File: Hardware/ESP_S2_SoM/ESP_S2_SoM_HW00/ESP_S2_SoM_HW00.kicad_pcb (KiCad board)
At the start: 2 copper layers, 21 x 26 mm, 53 parts, among them J101 USB4510-03-1-A, J102 54722-0604, SW401 SW_Push, SW402 SW_Push, U201 BQ24075RGTR, U301 MIC5528-3.3YMT-T5, U401 ESP32-S2FH4, Y601 Crystal_GND24_Small

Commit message: working on schematic
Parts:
- moved TP201 39.0 mm to (178.0, 49.0)
- moved SW401 16.3 mm to (176.7, 31.5)
- moved SW402 16.3 mm to (176.7, 35.2)
- moved Y601 16.3 mm to (177.7, 38.2)
- moved ANT401 16.3 mm to (171.0, 35.0)
- moved C409 16.3 mm to (174.6, 38.1)
- moved J101 11.2 mm to (158.6, 37.0)
- moved U401 1.41 mm to (161.1, 47.3), turned to -90 degrees
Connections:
- J102 pad 17: unconnected-(J102-Pad17) -> GND
- J102 pad 19: unconnected-(J102-Pad19) -> /100_Connectors/SPID
- J102 pad 21: unconnected-(J102-Pad21) -> /100_Connectors/SPIQ
- J102 pad 23: unconnected-(J102-Pad23) -> /100_Connectors/SPICLK
- J102 pad 25: unconnected-(J102-Pad25) -> /100_Connectors/SPICS0
- J102 pad 27: unconnected-(J102-Pad27) -> /100_Connectors/SPIWP
- J102 pad 29: unconnected-(J102-Pad29) -> /100_Connectors/SPIHD
- J102 pad 31: unconnected-(J102-Pad31) -> /100_Connectors/VDD_SPI
- J102 pad 33: unconnected-(J102-Pad33) -> /100_Connectors/SPICS1
- J102 pad 35: unconnected-(J102-Pad35) -> GND
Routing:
- net /400_ESP32/SPIHD: track 0.00 -> 2.73 mm, vias 0 -> 1
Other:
- copper layers 2 -> 4

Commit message: lots of work on routing
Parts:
- removed TP201: TestPoint, TestPoint:TestPoint_Pad_D1.0mm
- added R1: R, Resistor_SMD:R_0402_1005Metric, F.Cu at (156.2, 52.4)
- added REF**: usb-c-pcb, Component_lib:usb-c-pcb, B.Cu at (166.1, 32.1)
- C403, C404, C405, C408, C411, C412, C414, C415, C416: footprint Capacitor_SMD:C_0402_1005Metric -> Capacitor_SMD:C_0201_0603Metric
- R101, R102: moved to B.Cu
- moved U301 19.9 mm to (155.7, 55.6), turned to 180 degrees
- moved C413 19.7 mm to (173.6, 53.5), turned to -90 degrees
- moved C412 18.9 mm to (172.7, 53.3), turned to -90 degrees
- moved C301 18.8 mm to (153.7, 55.7), turned to 90 degrees
- moved R201 18.7 mm to (155.8, 44.3)
- moved R202 18.6 mm to (155.8, 43.4)
- moved C409 18.5 mm to (161.7, 51.4), turned to -90 degrees
- moved R203 18.5 mm to (154.4, 45.9)
- moved R301 17.9 mm to (155.3, 54.3), turned to 180 degrees
- moved R101 17.5 mm to (156.7, 42.4), turned to 180 degrees
- moved C201 17.1 mm to (154.2, 48.3), turned to 90 degrees
- moved C403 16.9 mm to (170.8, 45.6), turned to 90 degrees
- moved C416 16.8 mm to (170.7, 55.3)
- moved C402 16.4 mm to (169.0, 43.3), turned to -90 degrees
- moved C202 15.4 mm to (157.0, 45.6), turned to 180 degrees
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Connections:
- C412 pad 1: /400_ESP32/VDD_SPI -> SPI6
- C413 pad 1: /400_ESP32/VDD_SPI -> SPI6
- J102 pad 11: GND -> /100_Connectors/BATTERY_TEMP
- J102 pad 13: /100_Connectors/RX0 -> GND
- J102 pad 15: /100_Connectors/TX0 -> /100_Connectors/RX0
- J102 pad 17: GND -> /100_Connectors/TX0
- J102 pad 19: /100_Connectors/SPID -> GND
- J102 pad 21: /100_Connectors/SPIQ -> SPI0
- J102 pad 23: /100_Connectors/SPICLK -> SPI1
- J102 pad 25: /100_Connectors/SPICS0 -> SPI2
- J102 pad 27: /100_Connectors/SPIWP -> SPI3
- J102 pad 29: /100_Connectors/SPIHD -> SPI4
- J102 pad 31: /100_Connectors/VDD_SPI -> SPI5
- J102 pad 33: /100_Connectors/SPICS1 -> SPI6
- J102 pad 35: GND -> SPI7
- J102 pad 37: IO34 -> GND
- J102 pad 39: IO35 -> IO34
- J102 pad 41: IO36 -> IO35
- J102 pad 43: IO37 -> IO36
- J102 pad 45: IO38 -> IO37
- J102 pad 47: IO39 -> IO38
- J102 pad 49: IO40 -> IO39
- J102 pad 51: IO41 -> IO40
- J102 pad 53: IO42 -> IO41
- J102 pad 54: IO33 -> GND
- J102 pad 55: GND -> IO42
- J102 pad 56: GND -> /100_Connectors/D-
- J102 pad 57: /100_Connectors/D- -> IO33
- U201 pad 1: /200_1S_Charger/BATTERY_TEMP -> /100_Connectors/BATTERY_TEMP
- U401 pad 29: /400_ESP32/SPICS1 -> SPI7
- U401 pad 30: /400_ESP32/VDD_SPI -> SPI6
- U401 pad 31: /400_ESP32/SPIHD -> SPI5
- U401 pad 32: /400_ESP32/SPIWP -> SPI4
- U401 pad 33: /400_ESP32/SPICS0 -> SPI3
- U401 pad 34: /400_ESP32/SPICLK -> SPI2
- U401 pad 35: /400_ESP32/SPIQ -> SPI1
- U401 pad 36: /400_ESP32/SPID -> SPI0
- Y601 pad 1: Net-(C401-Pad1) -> Net-(U401-XTAL_N)
- Y601 pad 3: Net-(U401-XTAL_N) -> Net-(C401-Pad1)
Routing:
- net IO0: track 0.00 -> 9.94 mm
- net IO1: track 0.00 -> 9.30 mm
- net IO2: track 0.00 -> 8.79 mm
- net IO3: track 0.00 -> 8.29 mm
- net IO4: track 0.00 -> 7.79 mm
- net +3V3: track 0.00 -> 7.35 mm, vias 0 -> 1
- net IO5: track 0.00 -> 7.29 mm
- net IO6: track 0.00 -> 6.78 mm
- net IO7: track 0.00 -> 6.28 mm
- net IO8: track 0.00 -> 5.77 mm
- net GND: track 0.00 -> 5.26 mm
- net IO9: track 0.00 -> 5.23 mm
- net Net-(U401-XTAL_N): track 0.00 -> 4.75 mm
- net /200_1S_Charger/TMR: track 0.00 -> 4.38 mm
- net /200_1S_Charger/VSYS: track 0.00 -> 3.41 mm
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- added copper zone on In1.Cu, net GND
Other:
- board size 21 x 26 mm -> 22 x 25.6 mm

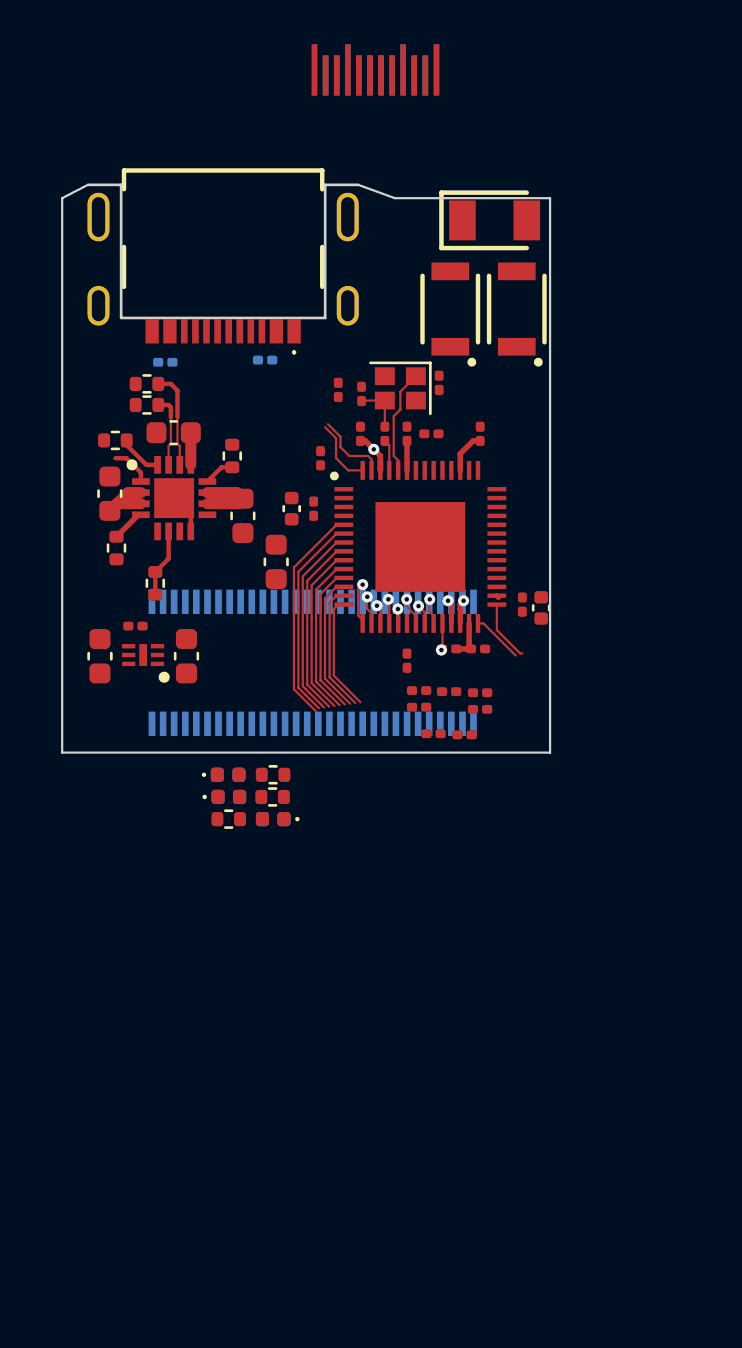
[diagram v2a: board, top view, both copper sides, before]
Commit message: led footprint update
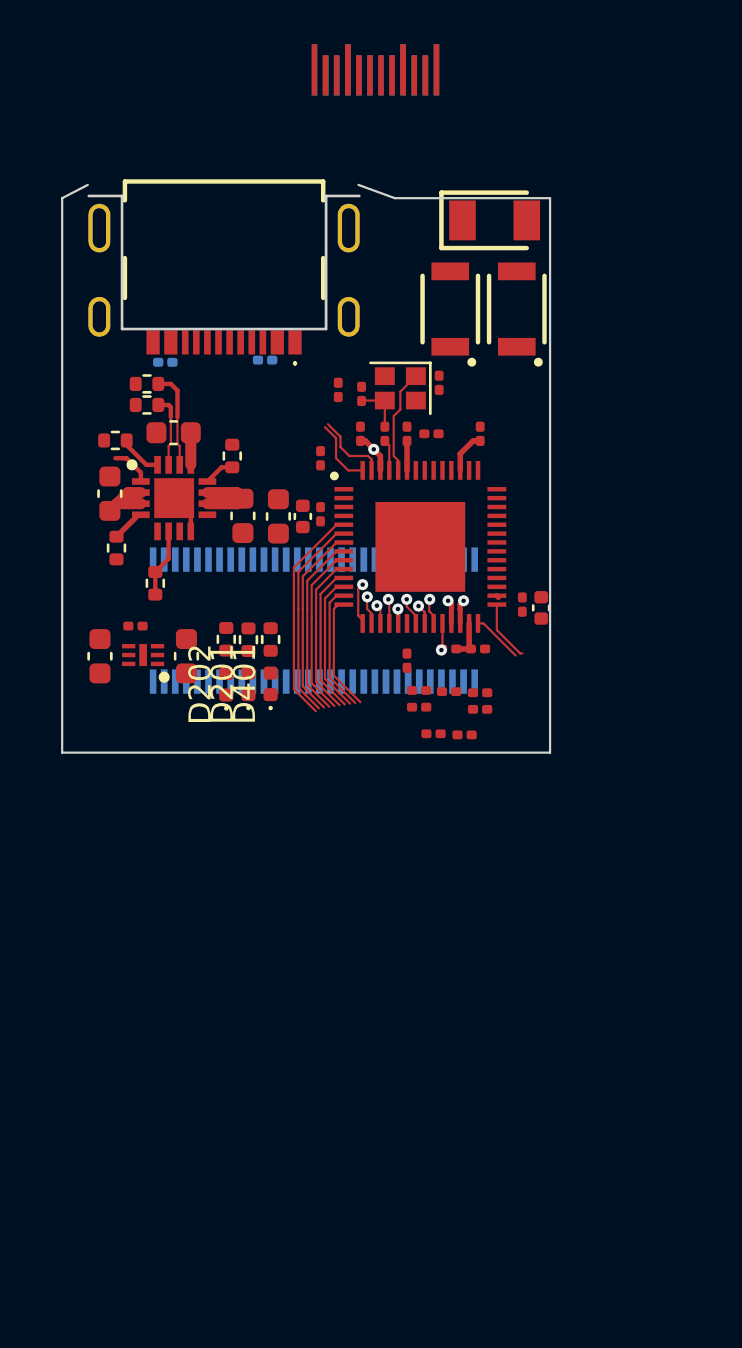
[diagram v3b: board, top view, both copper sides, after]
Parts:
- D201, D202, D401: footprint Component_lib:LED_0402_1005Metric_DUALSIDE -> LED_SMD:LED_0402_1005Metric
- moved R402 8.32 mm to (161.4, 54.9), turned to -90 degrees
- moved R205 7.17 mm to (160.4, 54.9), turned to -90 degrees
- moved R206 6.46 mm to (159.4, 54.9), turned to -90 degrees
- moved D401 6.10 mm to (161.4, 56.9), turned to 90 degrees
- moved D201 5.18 mm to (160.4, 56.9), turned to 90 degrees
- moved D202 4.09 mm to (159.4, 56.9), turned to 90 degrees
- moved C409 2.05 mm to (161.8, 49.4), turned to 90 degrees
- moved J102 1.90 mm to (163.3, 54.0)
- moved C410 0.61 mm to (162.8, 49.4)
- moved J101 0.50 mm to (159.3, 37.5)
- moved C411 0.40 mm to (163.7, 49.2)
